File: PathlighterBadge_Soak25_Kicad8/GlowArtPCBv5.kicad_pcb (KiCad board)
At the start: 2 copper layers, 93.2 x 113.9 mm, 13 parts, among them SW1 SW_SPDT

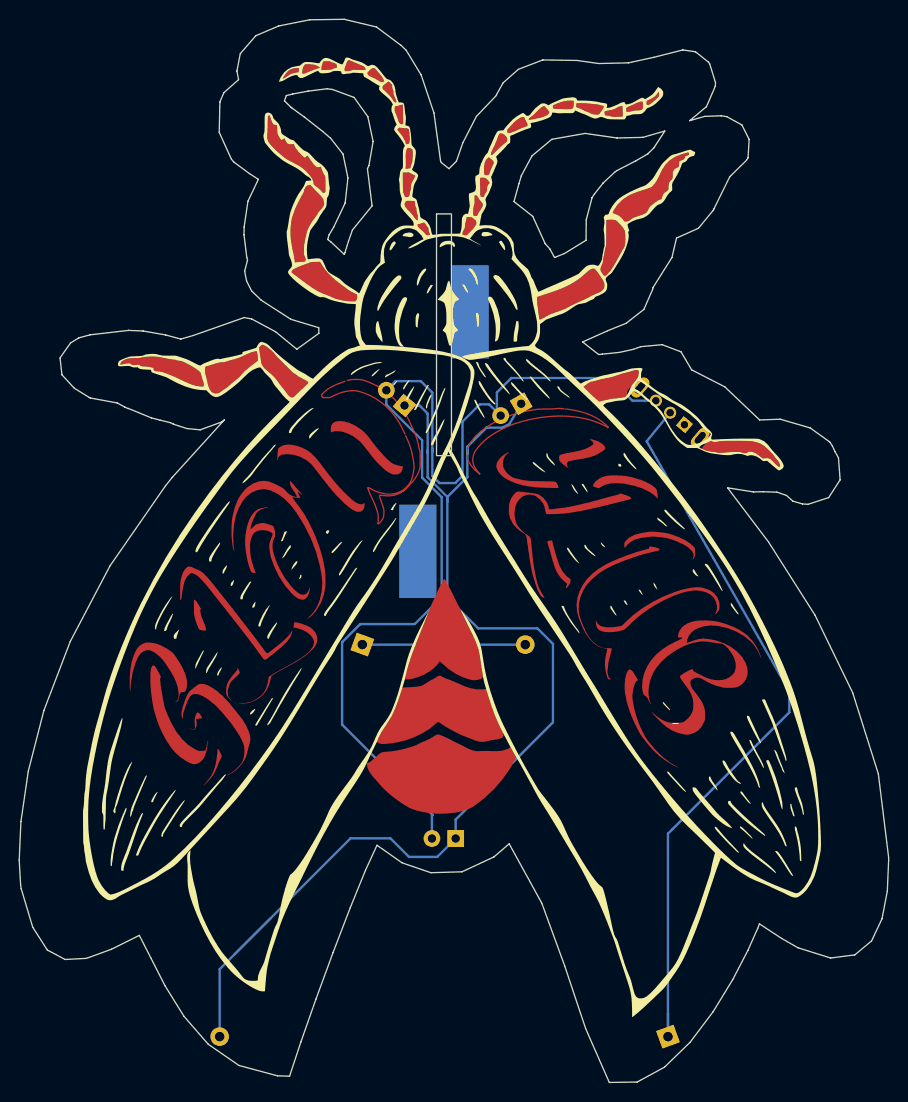
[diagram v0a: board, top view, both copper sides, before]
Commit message: Lots of little tweaks getting ready for production
Rerouting traces, baking board outlines without the weird bits,
adding silkscreen bits, generally polishing
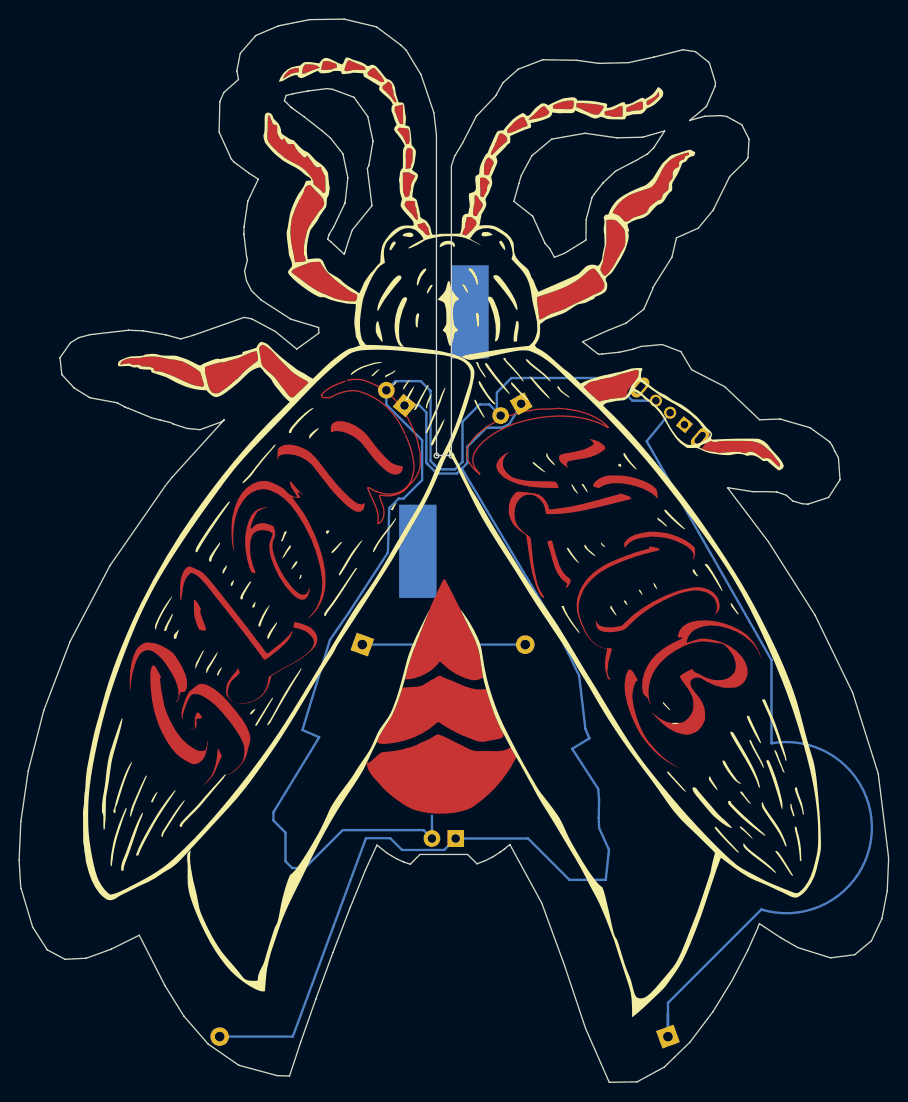
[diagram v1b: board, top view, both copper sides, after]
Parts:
- added REF**: NPTH_20mil, footprints:NPTH_20mil, F.Cu at (200.8, 88.2)
- added REF**: NPTH_20mil, footprints:NPTH_20mil, F.Cu at (199.2, 88.2)
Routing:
- net Net-(BT2-+): track 80.2 -> 63.2 mm
- net Net-(D1-A): track 114.0 -> 126.9 mm
- net Net-(BT1--): track 123.2 -> 131.7 mm
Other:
- outline, holes or cut-outs redrawn
- board text added: "+"
- board text added: "-"

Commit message: More final tweaks of some sort
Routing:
- net Net-(D1-A): track 126.9 -> 124.4 mm
